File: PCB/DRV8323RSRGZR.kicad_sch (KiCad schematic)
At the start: 39 parts, among them Q10 TPH3R704PL, Q11 TPH3R704PL, Q12 TPH3R704PL, Q7 TPH3R704PL, Q8 TPH3R704PL, Q9 TPH3R704PL, U2 TLV76733DRVR, U7 DRV8323RSRGZR

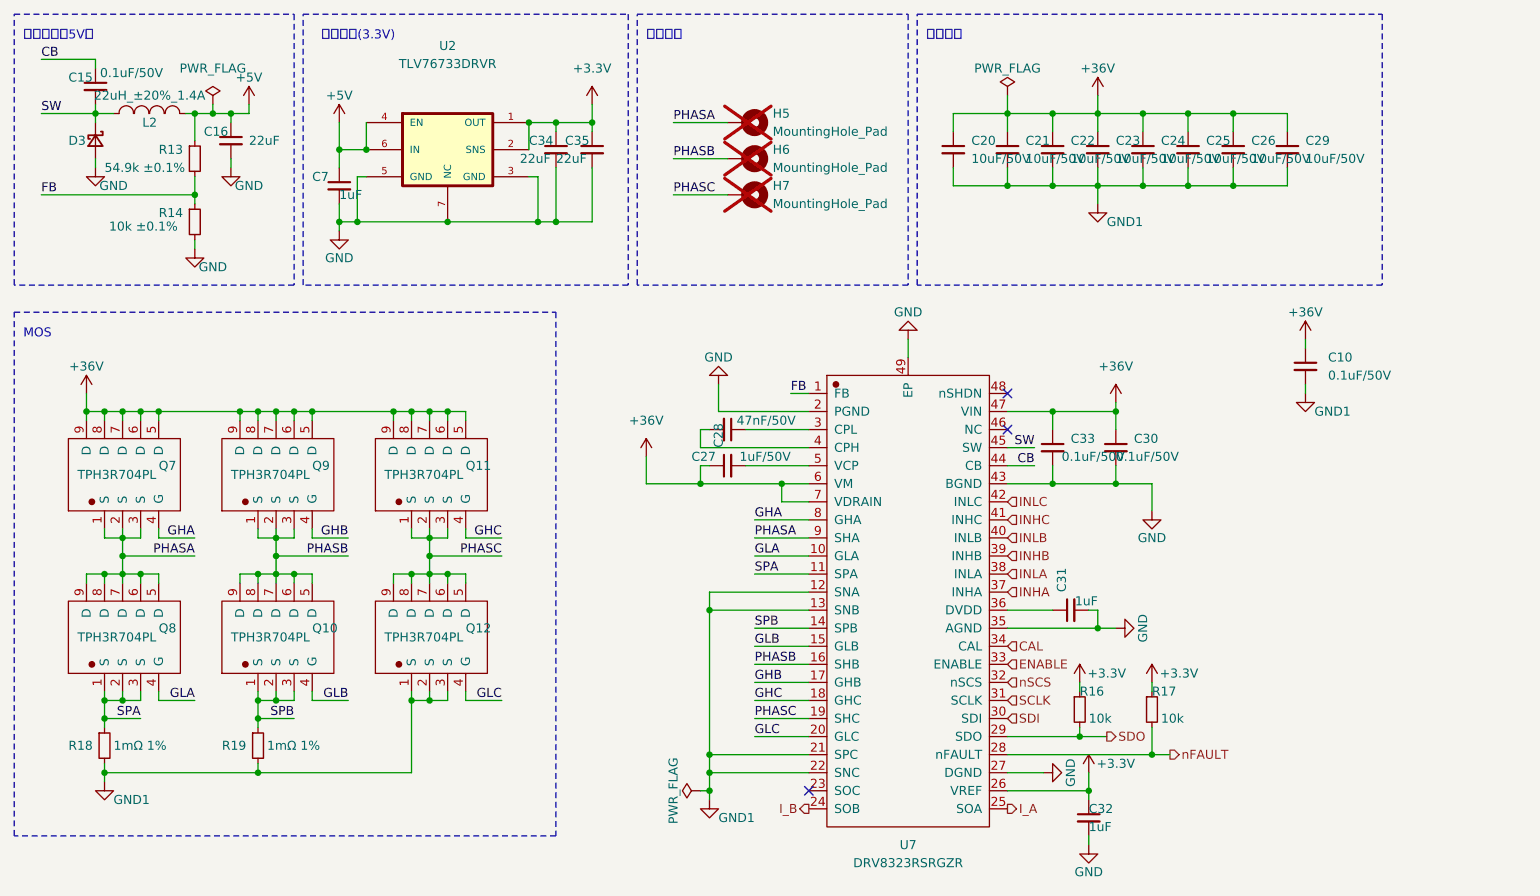
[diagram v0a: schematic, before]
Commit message: 升级V2版，支持3路电流采样以及霍尔传感器
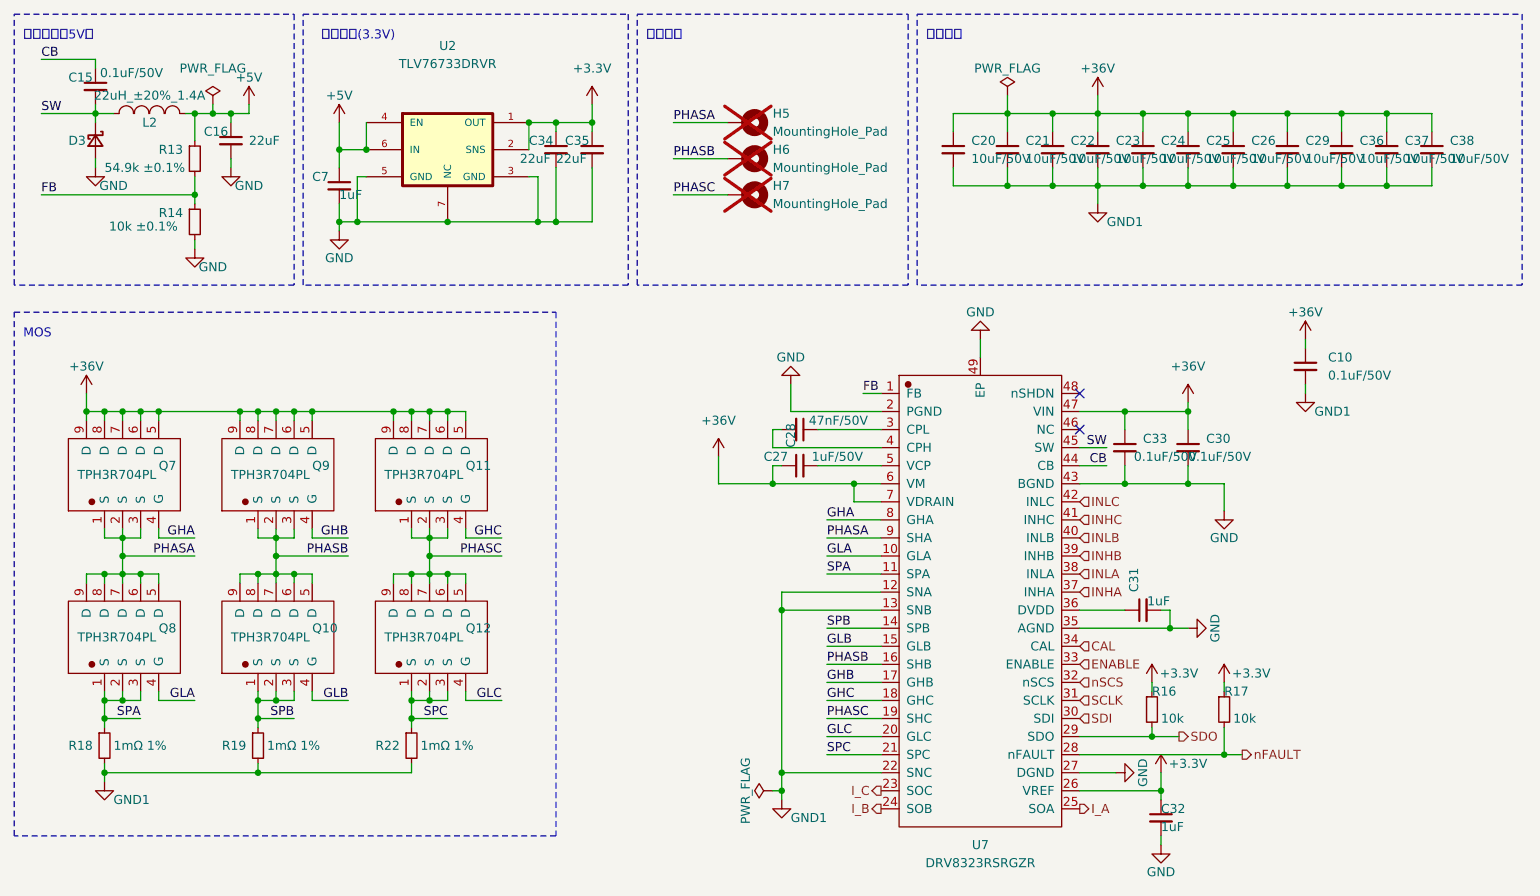
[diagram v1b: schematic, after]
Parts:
- added C36, C37, C38: 10uF/50V, Capacitor_SMD:C_1206_3216Metric_Pad1.33x1.80mm_HandSolder, symbol Device:C_Small
- added R22: 1mΩ 1%, Resistor_SMD:R_1210_3225Metric_Pad1.30x2.65mm_HandSolder, symbol Device:R_Small
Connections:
- net +36V: now also C36.1, C37.1, C38.1
- net GND1: now also C36.2, C37.2, C38.2, R22.2; no longer Q12.1 (S), Q12.2 (S), Q12.3 (S), U7.21 (SPC)
- net I_C: now reaches U7.23 (SOC)
- new net SPC: Q12.1 (S), Q12.2 (S), Q12.3 (S), R22.1, U7.21 (SPC)
- no-connect marks 3 -> 2
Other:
- moved on the sheet: C27, C28, C30, C31, C32, C33, R16, R17, U7

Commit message: 更新README
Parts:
- R18, R19, R22: value 1mΩ 1% -> 5mΩ 1%
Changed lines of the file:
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@@
 			)
 		)
-		(property "Value" "1mΩ 1%"
+		(property "Value" "5mΩ 1%"
 			(at 86.36 134.62 0)
 			(effects
@@
 			)
 		)
-		(property "Value" "1mΩ 1%"
+		(property "Value" "5mΩ 1%"
 			(at 64.77 134.62 0)
 			(effects
@@
 			)
 		)
-		(property "Value" "1mΩ 1%"
+		(property "Value" "5mΩ 1%"
 			(at 107.95 134.62 0)
 			(effects

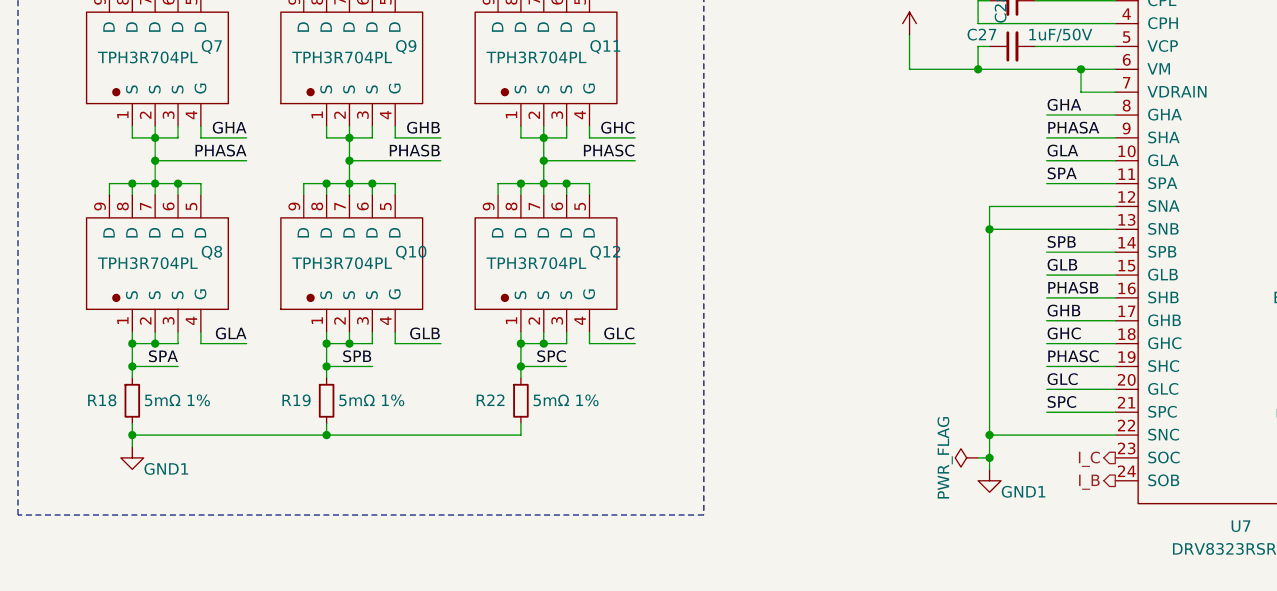
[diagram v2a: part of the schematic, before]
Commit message: 优化ADC采样布线
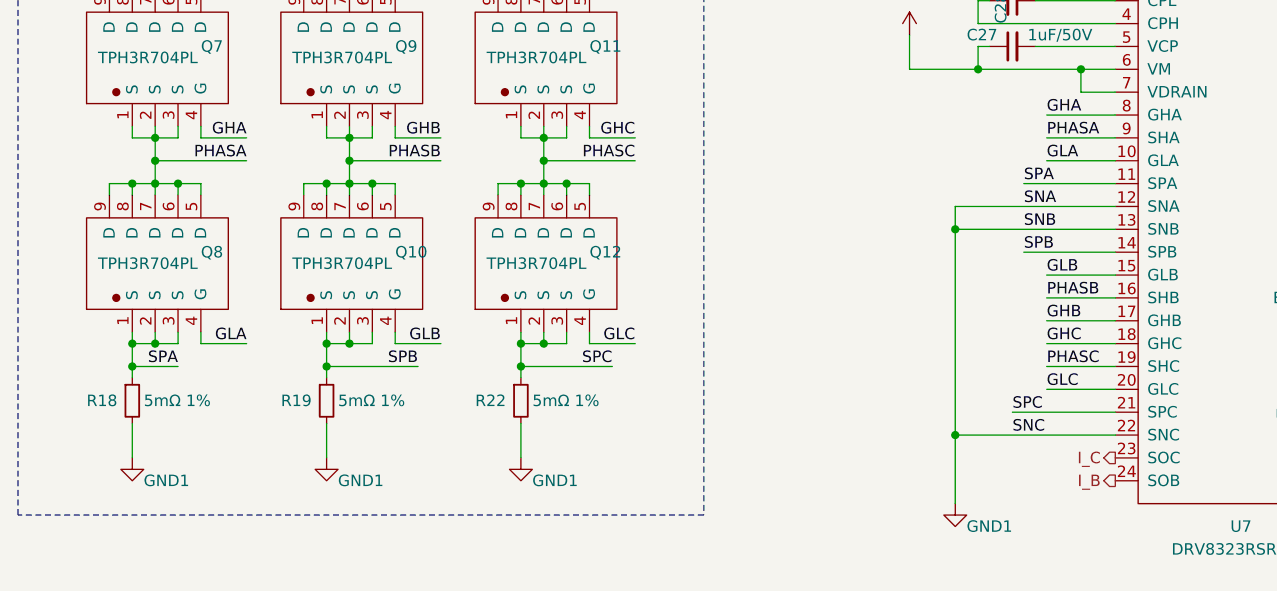
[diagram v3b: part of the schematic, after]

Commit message: 优化PCB
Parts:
- removed R22: 5mΩ 1%, Resistor_SMD:R_1210_3225Metric_Pad1.30x2.65mm_HandSolder, symbol Device:R_Small
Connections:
- net SPC is gone; now on net GND1: Q12.1 (S), Q12.2 (S), Q12.3 (S), U7.21 (SPC)
- net I_C: no longer names the net of U7.23 (SOC)
- no-connect marks 2 -> 3
